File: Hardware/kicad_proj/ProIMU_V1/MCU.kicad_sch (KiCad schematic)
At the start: 12 parts, among them J1 Conn_02x03_Counter_Clockwise, J2 502570-0893, U10 STM32F412RETx

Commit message: Added New USB footprint. This will be used through entire project and will not be changed
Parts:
- removed C1, C16, C17, C18, C19, C20: 1uF, Capacitor_SMD:C_0402_1005Metric_Pad0.74x0.62mm_HandSolder, symbol Device:C_Small
- removed C3: 100nF, Capacitor_SMD:C_0402_1005Metric_Pad0.74x0.62mm_HandSolder, symbol Device:C_Small
- removed J1: Conn_02x03_Counter_Clockwise, Connector_PinHeader_2.54mm:PinHeader_2x03_P2.54mm_Vertical_SMD, symbol Connector_Generic:Conn_02x03_Counter_Clockwise
- removed J2: 502570-0893, footprints:MOLEX_502570-0893, symbol 502570-0893:502570-0893
- removed R11, R3: 10K, Resistor_SMD:R_0402_1005Metric_Pad0.72x0.64mm_HandSolder, symbol Device:R_Small
- removed U10: STM32F412RETx, Package_QFP:LQFP-64_10x10mm_P0.5mm, symbol MCU_ST_STM32F4:STM32F412RETx
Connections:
- no-connect marks 1 -> 0

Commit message: Updated schematic and layout
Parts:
- added C17, C18, C19, C20, C21, C22: 1uF, Capacitor_SMD:C_0402_1005Metric_Pad0.74x0.62mm_HandSolder, symbol Device:C_Small
- added R11, R12: 10K, Resistor_SMD:R_0402_1005Metric_Pad0.72x0.64mm_HandSolder, symbol Device:R_Small
- added U8: STM32F411CEUx, Package_DFN_QFN:QFN-48-1EP_7x7mm_P0.5mm_EP5.6x5.6mm, symbol MCU_ST_STM32F4:STM32F411CEUx
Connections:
- new net: C17.1, U8.22 (VCAP1)
- new net: R11.2, U8.44 (BOOT0)
- new net +3V3: C18.1, C19.1, C20.1, C21.1, C22.1, R11.1, R12.2, U8.1 (VBAT), U8.24 (VDD), U8.36 (VDD), U8.48 (VDD), U8.9 (VDDA)
- new net GND: C17.2, C18.2, C19.2, C20.2, C21.2, C22.2, U8.23 (VSS), U8.35 (VSS), U8.47 (VSS), U8.49 (VSS), U8.8 (VSSA)
- new net NRST: R12.1, U8.7 (NRST)
- no-connect marks 0 -> 1

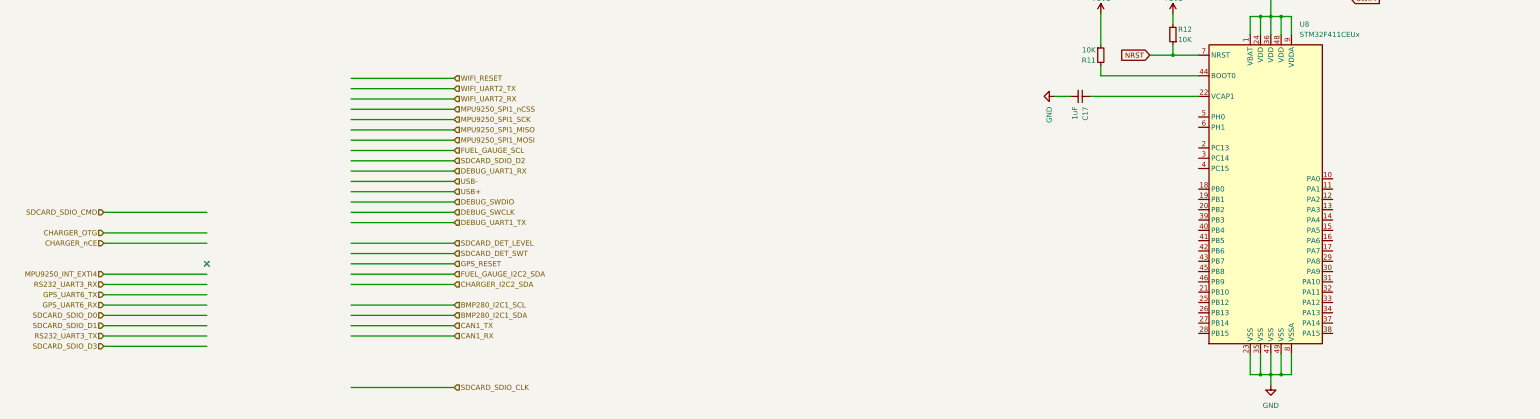
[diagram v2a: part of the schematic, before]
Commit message: Added a completed GPS V1 Schematic
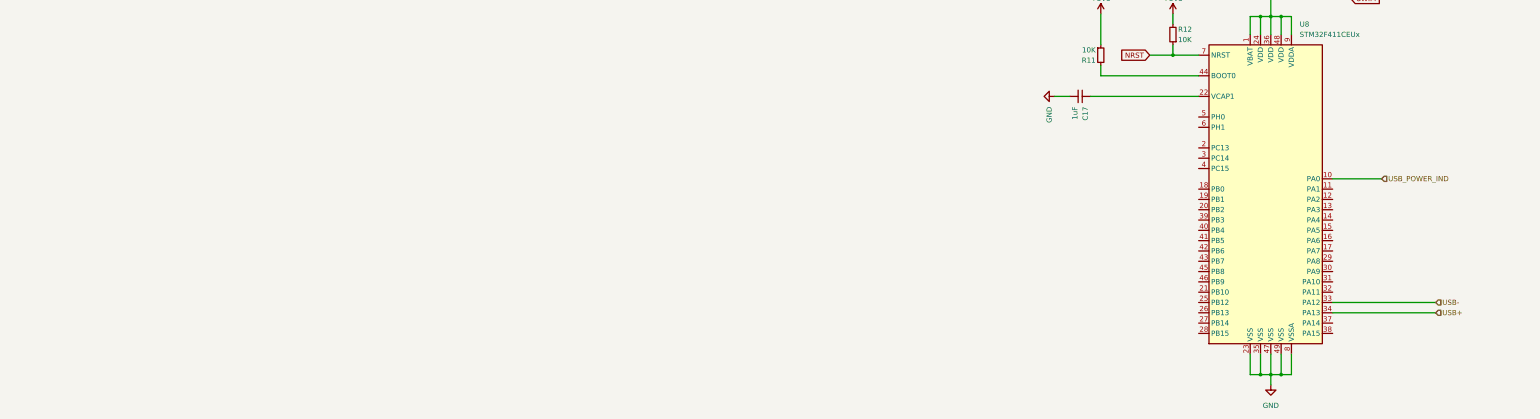
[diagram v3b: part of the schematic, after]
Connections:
- net USB+: now also U8.34 (PA13)
- net USB-: now also U8.33 (PA12)
- net USB_POWER_IND: now reaches U8.10 (PA0)
- no-connect marks 1 -> 0

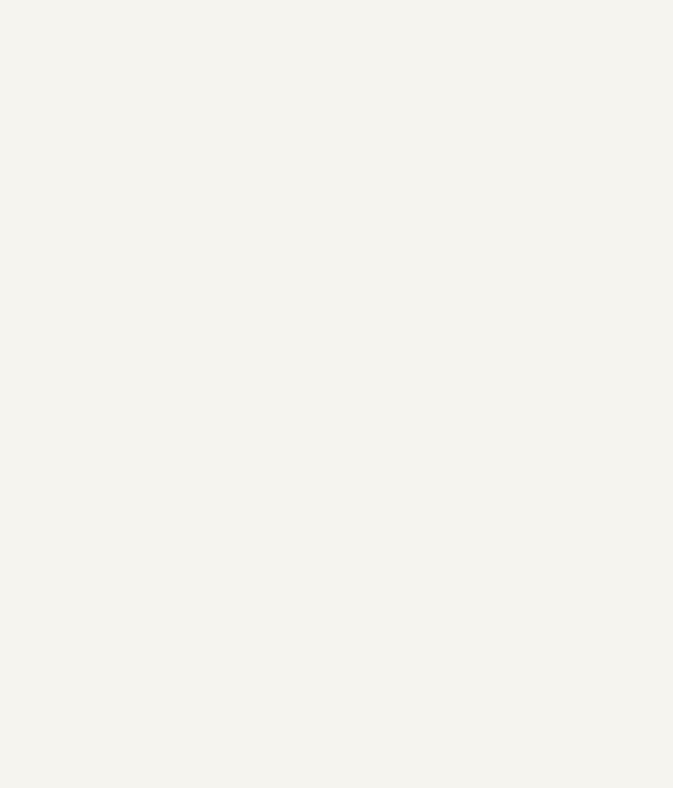
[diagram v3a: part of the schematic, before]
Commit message: Added GPS, LoRa and Wifi v1 schematic blocks
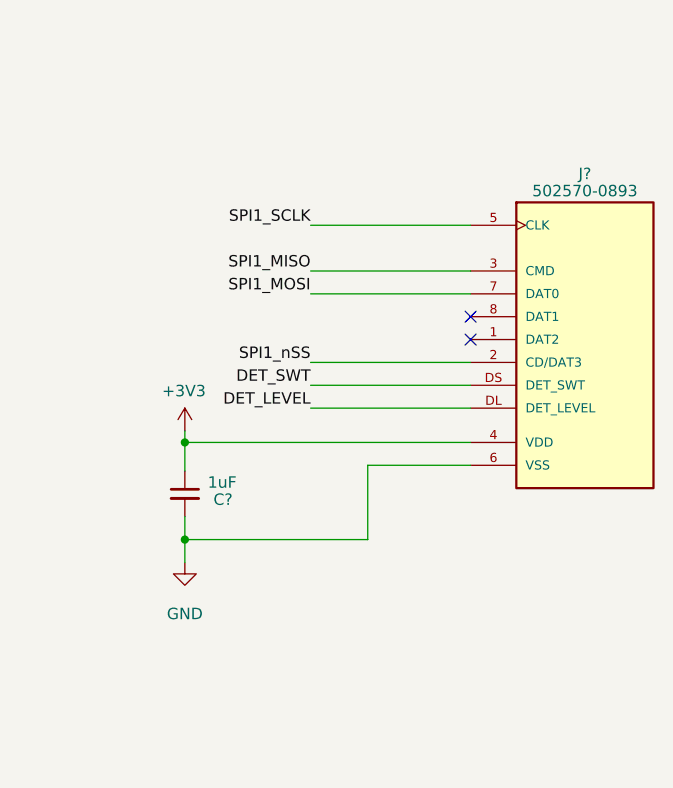
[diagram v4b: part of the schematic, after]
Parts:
- added C?: 1uF, Capacitor_SMD:C_0402_1005Metric_Pad0.74x0.62mm_HandSolder, symbol Device:C_Small
- added J?: 502570-0893, footprints:MOLEX_502570-0893, symbol 502570-0893:502570-0893
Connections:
- net +3V3: now also C?.1, J?.4 (VDD)
- net GND: now also C?.2, J?.6 (VSS)
- new net DET_LEVEL: J?.DL (DET_LEVEL)
- new net DET_SWT: J?.DS (DET_SWT)
- new net SPI1_MISO: J?.3 (CMD)
- new net SPI1_MOSI: J?.7 (DAT0)
- new net SPI1_SCLK: J?.5 (CLK)
- new net SPI1_nSS: J?.2 (CD/DAT3)
- no-connect marks 0 -> 2
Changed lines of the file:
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@@
   (junction (at 221.615 35.56) (diameter 0) (color 0 0 0 0)
   )
+  (junction (at 210.185 111.125) (diameter 0) (color 0 0 0 0)
+  )
+  (junction (at 210.185 121.92) (diameter 0) (color 0 0 0 0)
+  )
   (junction (at 113.665 72.39) (diameter 0) (color 0 0 0 0)
   )
@@
   (junction (at 135.255 62.865) (diameter 0) (color 0 0 0 0)
   )
+  (no_connect (at 241.935 97.155))
+  (no_connect (at 241.935 99.695))
   (wire (pts (xy 135.255 62.865) (xy 132.715 62.865))
     (stroke (width 0) (type default) (color 0 0 0 0))
@@
     (stroke (width 0) (type default) (color 0 0 0 0))
   )
+  (wire (pts (xy 210.185 121.92) (xy 210.185 124.46))
+    (stroke (width 0) (type default) (color 0 0 0 0))
+  )
   (wire (pts (xy 249.555 44.45) (xy 249.555 48.26))
     (stroke (width 0) (type default) (color 0 0 0 0))
@@
     (stroke (width 0) (type default) (color 0 0 0 0))
   )
+  (wire (pts (xy 230.505 121.92) (xy 210.185 121.92))
+    (stroke (width 0) (type default) (color 0 0 0 0))
+  )
+  (wire (pts (xy 210.185 119.38) (xy 210.185 121.92))
+    (stroke (width 0) (type default) (color 0 0 0 0))
+  )
   (wire (pts (xy 135.255 62.865) (xy 135.255 67.31))
     (stroke (width 0) (type default) (color 0 0 0 0))
@@
     (stroke (width 0) (type default) (color 0 0 0 0))
   )
+  (wire (pts (xy 241.935 113.665) (xy 230.505 113.665))
+    (stroke (width 0) (type default) (color 0 0 0 0))
+  )
   (wire (pts (xy 132.715 62.865) (xy 132.715 67.31))
     (stroke (width 0) (type default) (color 0 0 0 0))
@@
     (stroke (width 0) (type default) (color 0 0 0 0))
   )
+  (wire (pts (xy 224.155 102.235) (xy 241.935 102.235))
+    (stroke (width 0) (type default) (color 0 0 0 0))
+  )
   (wire (pts (xy 153.035 133.35) (xy 178.435 133.35))
     (stroke (width 0) (type default) (color 0 0 0 0))
@@
     (stroke (width 0) (type default) (color 0 0 0 0))
   )
+  (wire (pts (xy 210.185 111.125) (xy 210.185 114.3))
+    (stroke (width 0) (type default) (color 0 0 0 0))
+  )
   (wire (pts (xy 211.455 39.37) (xy 211.455 35.56))
     (stroke (width 0) (type default) (color 0 0 0 0))
@@
     (stroke (width 0) (type default) (color 0 0 0 0))
   )
+  (wire (pts (xy 230.505 113.665) (xy 230.505 121.92))
+    (stroke (width 0) (type default) (color 0 0 0 0))
+  )
   (wire (pts (xy 137.795 62.865) (xy 137.795 67.31))
     (stroke (width 0) (type default) (color 0 0 0 0))
@@
     (stroke (width 0) (type default) (color 0 0 0 0))
   )
+  (wire (pts (xy 224.155 92.075) (xy 241.935 92.075))
+    (stroke (width 0) (type default) (color 0 0 0 0))
+  )
   (wire (pts (xy 95.885 77.47) (xy 95.885 74.93))
     (stroke (width 0) (type default) (color 0 0 0 0))
@@
     (stroke (width 0) (type default) (color 0 0 0 0))
   )
+  (wire (pts (xy 224.155 86.995) (xy 241.935 86.995))
+    (stroke (width 0) (type default) (color 0 0 0 0))
+  )
+  (wire (pts (xy 224.155 104.775) (xy 241.935 104.775))
+    (stroke (width 0) (type default) (color 0 0 0 0))
+  )
   (wire (pts (xy 231.775 51.435) (xy 231.775 48.26))
     (stroke (width 0) (type default) (color 0 0 0 0))
@@
     (stroke (width 0) (type default) (color 0 0 0 0))
   )
+  (wire (pts (xy 241.935 111.125) (xy 210.185 111.125))
+    (stroke (width 0) (type default) (color 0 0 0 0))
+  )
   (wire (pts (xy 137.795 56.515) (xy 137.795 62.865))
     (stroke (width 0) (type default) (color 0 0 0 0))
   )
+  (wire (pts (xy 224.155 94.615) (xy 241.935 94.615))
+    (stroke (width 0) (type default) (color 0 0 0 0))
+  )
   (wire (pts (xy 135.255 146.05) (xy 135.255 151.13))
     (stroke (width 0) (type default) (color 0 0 0 0))
@@
     (stroke (width 0) (type default) (color 0 0 0 0))
   )
+  (wire (pts (xy 210.185 111.125) (xy 210.185 109.855))
+    (stroke (width 0) (type default) (color 0 0 0 0))
+  )
+  (wire (pts (xy 224.155 107.315) (xy 241.935 107.315))
+    (stroke (width 0) (type default) (color 0 0 0 0))
+  )
   (wire (pts (xy 137.795 151.13) (xy 137.795 153.67))
     (stroke (width 0) (type default) (color 0 0 0 0))
@@
   (wire (pts (xy 221.615 39.37) (xy 221.615 35.56))
     (stroke (width 0) (type default) (color 0 0 0 0))
+  )
+  (label "SPI1_MISO" (at 224.155 92.075 180)
+    (effects (font (size 1.27 1.27)) (justify right bottom))
+  )
+  (label "DET_LEVEL" (at 224.155 107.315 180)
+    (effects (font (size 1.27 1.27)) (justify right bottom))
+  )
+  (label "SPI1_SCLK" (at 224.155 86.995 180)
+    (effects (font (size 1.27 1.27)) (justify right bottom))
+  )
+  (label "SPI1_nSS" (at 224.155 102.235 180)
+    (effects (font (size 1.27 1.27)) (justify right bottom))
+  )
+  (label "SPI1_MOSI" (at 224.155 94.615 180)
+    (effects (font (size 1.27 1.27)) (justify right bottom))
+  )
+  (label "DET_SWT" (at 224.155 104.775 180)
+    (effects (font (size 1.27 1.27)) (justify right bottom))
   )
   (global_label "SWCLK" (shape input) (at 157.48 55.88 0) (fields_autoplaced)
@@
     (pin "2")
   )
+  (symbol (lib_id "power:+3V3") (at 210.185 109.855 0) (mirror y) (unit 1)
+    (in_bom yes) (on_board yes)
+    (property "Reference" "#PWR?" (id 0) (at 210.185 113.665 0)
+      (effects (font (size 1.27 1.27)) hide)
+    )
+    (property "Value" "+3V3" (id 1) (at 207.645 105.41 0)
+      (effects (font (size 1.27 1.27)) (justify right))
+    )
+    (property "Footprint" "" (id 2) (at 210.185 109.855 0)
+      (effects (font (size 1.27 1.27)) hide)
+    )
+    (property "Datasheet" "" (id 3) (at 210.185 109.855 0)
+      (effects (font (size 1.27 1.27)) hide)
+    )
+    (pin "1")
+  )
   (symbol (lib_id "power:GND") (at 84.455 82.55 270) (unit 1)
     (in_bom yes) (on_board yes)
@@
     (pin "1")
   )
+  (symbol (lib_id "502570-0893:502570-0893") (at 259.715 97.155 0) (unit 1)
+    (in_bom yes) (on_board yes)
+    (property "Reference" "J?" (id 0) (at 254.635 81.28 0))
+    (property "Value" "502570-0893" (id 1) (at 254.635 83.185 0))
+    (property "Footprint" "footprints:MOLEX_502570-0893" (id 2) (at 259.715 97.155 0)
+      (effects (font (size 1.27 1.27)) (justify left bottom) hide)
+    )
+    (property "Datasheet" "" (id 3) (at 259.715 97.155 0)
+      (effects (font (size 1.27 1.27)) (justify left bottom) hide)
+    )
+    (pin "1")
+    (pin "2")
+    (pin "3")
+    (pin "4")
+    (pin "5")
+    (pin "6")
+    (pin "7")
+    (pin "8")
+    (pin "DL")
+    (pin "DS")
+  )
   (symbol (lib_id "power:+3V3") (at 231.775 32.385 0) (unit 1)
     (in_bom yes) (on_board yes)
@@
     )
     (property "Datasheet" "" (id 3) (at 231.775 32.385 0)
+      (effects (font (size 1.27 1.27)) hide)
+    )
+    (pin "1")
+  )
+  (symbol (lib_id "power:GND") (at 210.185 124.46 0) (mirror y) (unit 1)
+    (in_bom yes) (on_board yes) (fields_autoplaced)
+    (property "Reference" "#PWR?" (id 0) (at 210.185 130.81 0)
+      (effects (font (size 1.27 1.27)) hide)
+    )
+    (property "Value" "GND" (id 1) (at 210.185 130.175 0))
+    (property "Footprint" "" (id 2) (at 210.185 124.46 0)
+      (effects (font (size 1.27 1.27)) hide)
+    )
+    (property "Datasheet" "" (id 3) (at 210.185 124.46 0)
       (effects (font (size 1.27 1.27)) hide)
     )
@@
       (effects (font (size 1.27 1.27)) hide)
     )
+    (pin "1")
+    (pin "2")
+  )
+  (symbol (lib_id "Device:C_Small") (at 210.185 116.84 0) (mirror y) (unit 1)
+    (in_bom yes) (on_board yes)
+    (property "Reference" "C?" (id 0) (at 213.36 117.475 0)
+      (effects (font (size 1.27 1.27)) (justify right))
+    )
+    (property "Value" "1uF" (id 1) (at 212.725 115.57 0)
+      (effects (font (size 1.27 1.27)) (justify right))
+    )
+    (property "Footprint" "Capacitor_SMD:C_0402_1005Metric_Pad0.74x0.62mm_HandSolder" (id 2) (at 210.185 116.84 0)
+      (effects (font (size 1.27 1.27)) hide)
+    )
+    (property "Datasheet" "~" (id 3) (at 210.185 116.84 0)
+      (effects (font (size 1.27 1.27)) hide)
+    )
